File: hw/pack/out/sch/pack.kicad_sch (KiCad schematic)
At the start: 0 parts

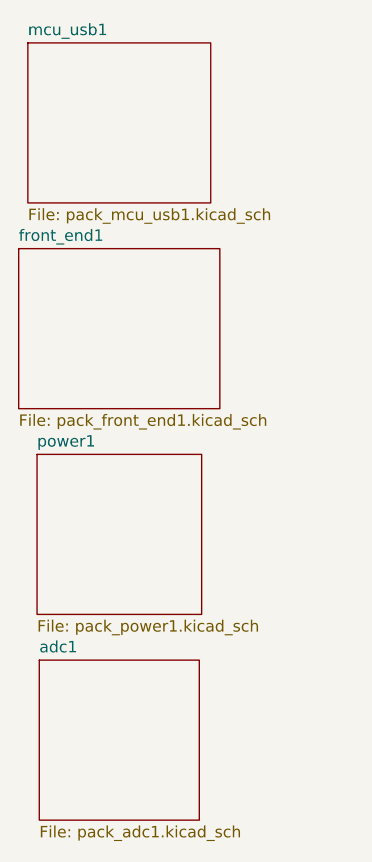
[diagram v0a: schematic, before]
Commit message: hw/pack: review fixes for #75 (op-amp CM, hot-plug protection, CI, cutoff, LEDs) (#31)
- VCM 180k/100k (1.77 V) keeps OPA1656 +IN inside V+ - 2.25 V; SPICE clamp 0.25/4.70 V,
  test asserts input CM, ADC pin (1.375 V) and prints numbers in CI (-rP)
- tip ESD (TPD1E10B06), BAV199 clamp + 100R ahead of the op-amp; C9 22p; noise 0.96 uV
- CI installs skidl==3.0.0, pack test fails (not skips) under CI, stale-output diff check
- no PTC; cell sensed at BAT+; firmware cutoff 3.2 V derived in audit.py; PK-8 LED
  thresholds -10/-7 dBFS; real LED MPNs; VDDH decoupling; audit prints DK-price BOM

Co-Authored-By: Claude Opus 5.5 <noreply@anthropic.com>
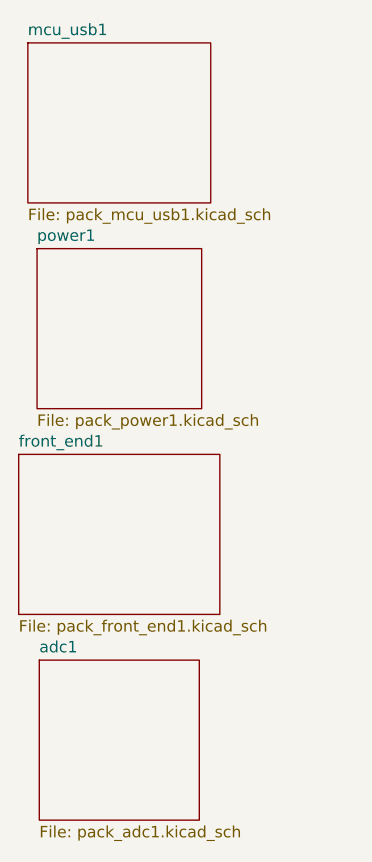
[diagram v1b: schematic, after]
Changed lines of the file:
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@@
     (comment 4 ""))
   (sheet
-    (at 139.45 107.95)
+    (at 139.45 85.09)
     (size 18.29 17.78)
     (exclude_from_sim no)
@@
       (color 0 0 0 0.0))
     (property "Sheetname" "power1"
-      (at 139.45 107.24 0)
+      (at 139.45 84.38 0)
       (effects
         (font
@@
         (justify left bottom)))
     (property "Sheetfile" "pack_power1.kicad_sch"
-      (at 139.45 126.31 0)
+      (at 139.45 103.45 0)
       (effects
         (font
@@
         (justify left top))))
   (sheet
-    (at 137.41 85.09)
+    (at 137.41 107.95)
     (size 22.35 17.78)
     (exclude_from_sim no)
@@
       (color 0 0 0 0.0))
     (property "Sheetname" "front_end1"
-      (at 137.41 84.38 0)
+      (at 137.41 107.24 0)
       (effects
         (font
@@
         (justify left bottom)))
     (property "Sheetfile" "pack_front_end1.kicad_sch"
-      (at 137.41 103.45 0)
+      (at 137.41 126.31 0)
       (effects
         (font

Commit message: hw/pack: 3 A chip fuse (23 mOhm) on BAT+, cutoff re-derived, BOM $34.98 (#31)
Co-Authored-By: Claude Opus 5.5 <noreply@anthropic.com>
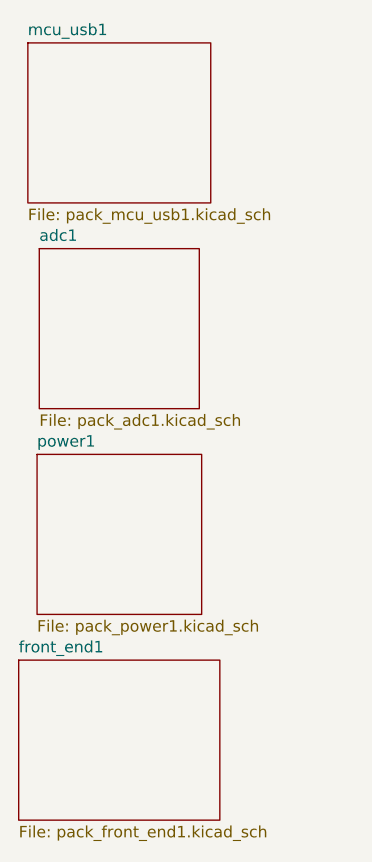
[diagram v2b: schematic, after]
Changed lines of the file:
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@@
     (comment 4 ""))
   (sheet
-    (at 139.45 85.09)
+    (at 139.45 107.95)
     (size 18.29 17.78)
     (exclude_from_sim no)
@@
       (color 0 0 0 0.0))
     (property "Sheetname" "power1"
-      (at 139.45 84.38 0)
+      (at 139.45 107.24 0)
       (effects
         (font
@@
         (justify left bottom)))
     (property "Sheetfile" "pack_power1.kicad_sch"
-      (at 139.45 103.45 0)
+      (at 139.45 126.31 0)
       (effects
         (font
@@
         (justify left top))))
   (sheet
-    (at 137.41 107.95)
+    (at 137.41 130.81)
     (size 22.35 17.78)
     (exclude_from_sim no)
@@
       (color 0 0 0 0.0))
     (property "Sheetname" "front_end1"
-      (at 137.41 107.24 0)
+      (at 137.41 130.1 0)
       (effects
         (font
@@
         (justify left bottom)))
     (property "Sheetfile" "pack_front_end1.kicad_sch"
-      (at 137.41 126.31 0)
+      (at 137.41 149.17 0)
       (effects
         (font
@@
         (justify left top))))
   (sheet
-    (at 139.7 130.81)
+    (at 139.7 85.09)
     (size 17.78 17.78)
     (exclude_from_sim no)
@@
       (color 0 0 0 0.0))
     (property "Sheetname" "adc1"
-      (at 139.7 130.1 0)
+      (at 139.7 84.38 0)
       (effects
         (font
@@
         (justify left bottom)))
     (property "Sheetfile" "pack_adc1.kicad_sch"
-      (at 139.7 149.17 0)
+      (at 139.7 103.45 0)
       (effects
         (font

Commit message: pack: restore battery-sense divider (R13/C30) (#84)
* hw/pack: restore battery-sense divider R13/C30 hidden in a comment

Co-Authored-By: Claude Sonnet 5.5 <noreply@anthropic.com>

* tests: cite nRF5340 SAADC pin limit (VDD) from the product spec

Co-Authored-By: Claude Sonnet 5.5 <noreply@anthropic.com>

* hw/pack: price 0402 resistors and 100n caps from LCSC qty-100 pages; UK BOM refs; merge main

Co-Authored-By: Claude Sonnet 5.5 <noreply@anthropic.com>

---------

Co-authored-by: Claude Sonnet 5.5 <noreply@anthropic.com>
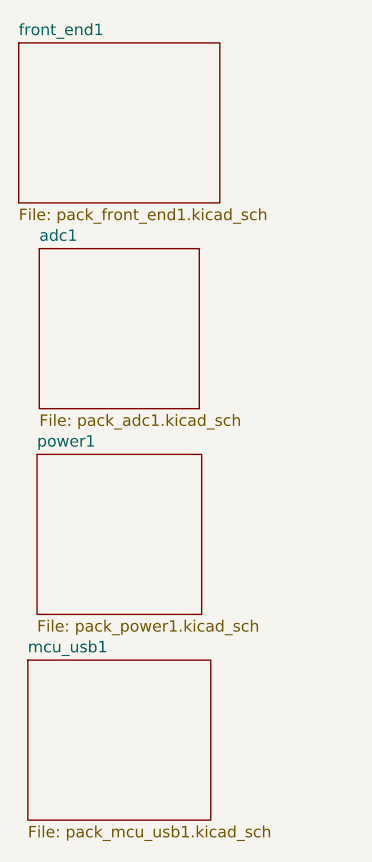
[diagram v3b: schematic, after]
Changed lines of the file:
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@@
         (justify left top))))
   (sheet
-    (at 137.41 130.81)
+    (at 137.41 62.23)
     (size 22.35 17.78)
     (exclude_from_sim no)
@@
       (color 0 0 0 0.0))
     (property "Sheetname" "front_end1"
-      (at 137.41 130.1 0)
+      (at 137.41 61.52 0)
       (effects
         (font
@@
         (justify left bottom)))
     (property "Sheetfile" "pack_front_end1.kicad_sch"
-      (at 137.41 149.17 0)
+      (at 137.41 80.59 0)
       (effects
         (font
@@
         (justify left top))))
   (sheet
-    (at 138.43 62.23)
+    (at 138.43 130.81)
     (size 20.32 17.78)
     (exclude_from_sim no)
@@
       (color 0 0 0 0.0))
     (property "Sheetname" "mcu_usb1"
-      (at 138.43 61.52 0)
+      (at 138.43 130.1 0)
       (effects
         (font
@@
         (justify left bottom)))
     (property "Sheetfile" "pack_mcu_usb1.kicad_sch"
-      (at 138.43 80.59 0)
+      (at 138.43 149.17 0)
       (effects
         (font

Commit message: hw/pack: 4-layer pack PCB layout, review fixes, fab outputs, cost-down (#104)
* hw/pack: scripted 4-layer layout from the netlist, DRC clean (#34)

layout.py builds pack.kicad_pcb from out/pack.net with pcbnew: outline from
mech/pack.py, BT40NE antenna past the board edge, TI-pattern boost cell,
grid maze router (router.py), GND fan-out vias, RF via fence, JLC rules in
pack.kicad_dru. outputs.py writes gerbers/drill/BOM/CPL/STEP and renders.

Co-Authored-By: Claude Opus 5.5 <noreply@anthropic.com>

* hw/pack: enclosure fit (fit.py + CadQuery test), mech outline from the layout, layout tests (#34)

mech/pack.py takes the real outline (73.4 x 35 mm, post notch), z0 +1.4 mm so
the module antenna clears the clip bosses, and the antenna overhang as a part.
fit.py checks board/parts/openings/lid features without CadQuery and renders
fit_top/fit_side.png; tests/mech/test_pack_fit.py does it with the STEP.
tests/test_pack_layout.py: DRC 0 errors, fab outputs fresh, netlist parity.

Co-Authored-By: Claude Opus 5.5 <noreply@anthropic.com>

* hw/REVIEW.md: pack board layout review, fixes and open items (#34)

Co-Authored-By: Claude Opus 5.5 <noreply@anthropic.com>

* hw/pack, mech: SJ1-3543 from datasheet, M2 board retention, light pipes, switch fork, CI pcb job (#34)

- SJ1-3543 footprint from Same Sky SJ1-354X (09/2024): 12x11.6x9.6 body, M6
  bushing through the wall from the inner face, axis 5.2 mm, anchors on GND
- H1/H2 M2 holes + printed pilot bosses (mech PCB_SCREWS), two rests
- lid light-pipe chimneys (lid prints outer-face-down), printed switch fork
  straddling SW1's right-angle actuator through a relocated slot
- mech comps() now the per-part envelope from the layout
- fit.py checks fork, chimneys, screws; CadQuery fit test mandatory under CI
- ci.yml: pcb job (KiCad 10 PPA) runs tests/test_pack_layout.py
- REVIEW: holder BH-18650-W and pigtail Molex 0731160017 chosen; with them
  PK-12 would be ~$38.2 > $35, prices.py left unchanged pending decision

Co-Authored-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
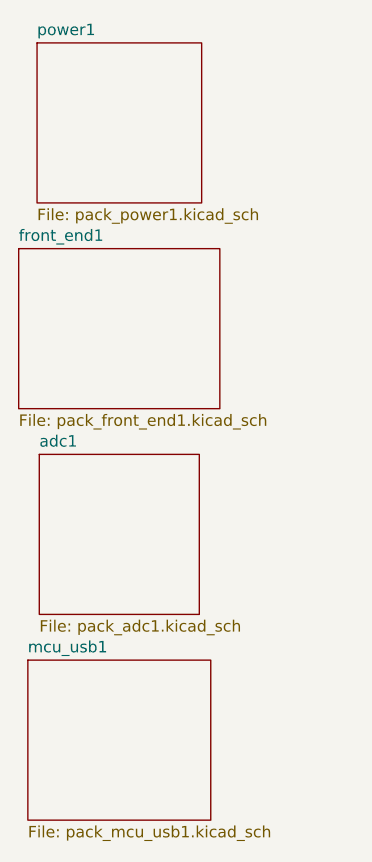
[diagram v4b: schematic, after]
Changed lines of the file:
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@@
   (title_block
     (title "OpenPack body-pack")
-    (date "2026-10-31")
+    (date "2026-11-01")
     (company "")
     (comment 1 "Generated with SKiDL")
@@
     (comment 4 ""))
   (sheet
-    (at 139.45 107.95)
+    (at 139.45 62.23)
     (size 18.29 17.78)
     (exclude_from_sim no)
@@
       (color 0 0 0 0.0))
     (property "Sheetname" "power1"
-      (at 139.45 107.24 0)
+      (at 139.45 61.52 0)
       (effects
         (font
@@
         (justify left bottom)))
     (property "Sheetfile" "pack_power1.kicad_sch"
-      (at 139.45 126.31 0)
+      (at 139.45 80.59 0)
       (effects
         (font
@@
         (justify left top))))
   (sheet
-    (at 137.41 62.23)
+    (at 137.41 85.09)
     (size 22.35 17.78)
     (exclude_from_sim no)
@@
       (color 0 0 0 0.0))
     (property "Sheetname" "front_end1"
-      (at 137.41 61.52 0)
+      (at 137.41 84.38 0)
       (effects
         (font
@@
         (justify left bottom)))
     (property "Sheetfile" "pack_front_end1.kicad_sch"
-      (at 137.41 80.59 0)
+      (at 137.41 103.45 0)
       (effects
         (font
@@
         (justify left top))))
   (sheet
-    (at 139.7 85.09)
+    (at 139.7 107.95)
     (size 17.78 17.78)
     (exclude_from_sim no)
@@
       (color 0 0 0 0.0))
     (property "Sheetname" "adc1"
-      (at 139.7 84.38 0)
+      (at 139.7 107.24 0)
       (effects
         (font
@@
         (justify left bottom)))
     (property "Sheetfile" "pack_adc1.kicad_sch"
-      (at 139.7 103.45 0)
+      (at 139.7 126.31 0)
       (effects
         (font
